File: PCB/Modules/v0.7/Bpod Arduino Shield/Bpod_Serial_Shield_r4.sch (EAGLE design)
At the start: 9 parts, among them IC1 SN65HVD31DR

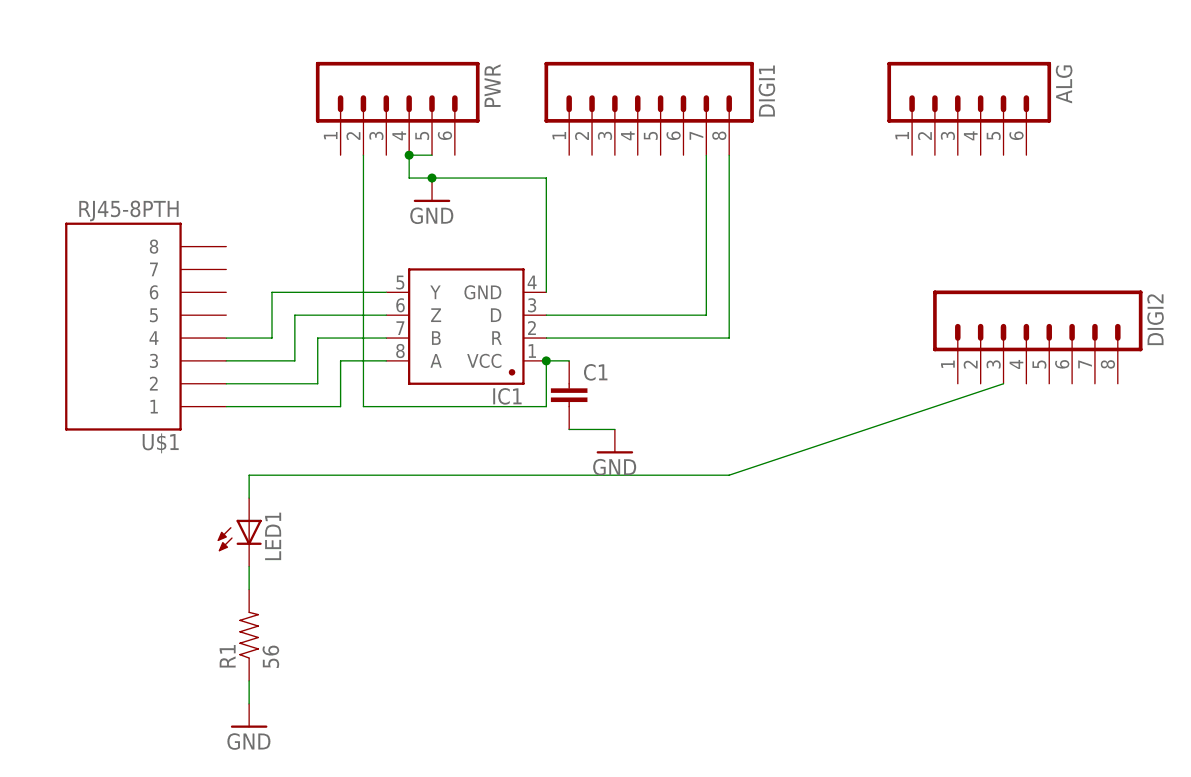
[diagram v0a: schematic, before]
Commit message: -Added design files for the Pocket State Machine - a new state machine module with many improvements, based on Teensy 3.6. -Added design files for isolated valve driver module -Added new revision of Bpod arduino shield, allowing modules to be powered from the Pocket State Machine (when they do not require a USB connection)
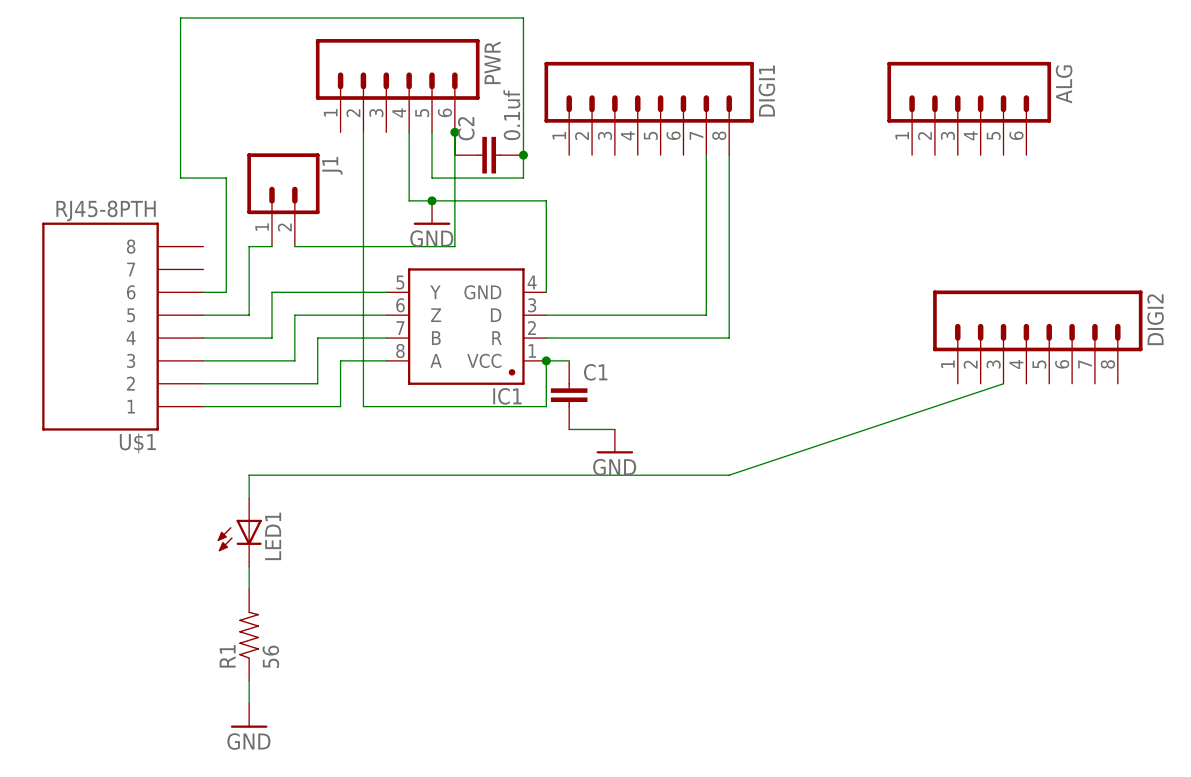
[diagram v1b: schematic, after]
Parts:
- added C2: 0.1uf, SparkFun-Capacitors:CAP1206
- added J1: (no value), SparkFun-Connectors:CONN_02
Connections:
- new net N$11: C2.2, PWR.5, U$1.6
- new net N$12: J1.1, U$1.5
- new net N$5: C2.1, J1.2, PWR.6
- net GND: no longer PWR.5
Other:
- moved on the sheet: PWR, U$1
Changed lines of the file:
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@@
 <?xml version="1.0" encoding="utf-8"?>
 <!DOCTYPE eagle SYSTEM "eagle.dtd">
-<eagle version="7.6.0">
+<eagle version="7.7.0">
 <drawing>
 <settings>
@@
 <layer number="112" name="tSilk" color="7" fill="1" visible="yes" active="yes"/>
 <layer number="113" name="IDFDebug" color="7" fill="1" visible="yes" active="yes"/>
+<layer number="114" name="Badge_Outline" color="7" fill="1" visible="yes" active="yes"/>
+<layer number="115" name="ReferenceISLANDS" color="7" fill="1" visible="yes" active="yes"/>
 <layer number="116" name="Patch_BOT" color="9" fill="4" visible="no" active="yes"/>
 <layer number="118" name="Rect_Pads" color="7" fill="1" visible="yes" active="yes"/>
@@
 <part name="LED1" library="adafruit" deviceset="LED" device="CHIPLED_1206"/>
 <part name="R1" library="SparkFun-Resistors" deviceset="RESISTOR" device="1206" value="56"/>
+<part name="J1" library="SparkFun-Connectors" deviceset="CONN_02" device=""/>
+<part name="C2" library="SparkFun-Capacitors" deviceset="CAP" device="1206" value="0.1uf"/>
 </parts>
 <sheets>
@@
 </plain>
 <instances>
-<instance part="PWR" gate="G$1" x="88.9" y="66.04" rot="R270"/>
+<instance part="PWR" gate="G$1" x="88.9" y="68.58" rot="R270"/>
 <instance part="ALG" gate="G$1" x="152.4" y="66.04" rot="R270"/>
 <instance part="DIGI1" gate="G$1" x="116.84" y="66.04" rot="R270"/>
 <instance part="DIGI2" gate="G$1" x="160.02" y="40.64" rot="R270"/>
-<instance part="U$1" gate="G$1" x="58.42" y="43.18" rot="R180"/>
-<instance part="GND1" gate="1" x="93.98" y="55.88"/>
+<instance part="U$1" gate="G$1" x="55.88" y="43.18" rot="R180"/>
+<instance part="GND1" gate="1" x="93.98" y="53.34"/>
 <instance part="GND2" gate="1" x="73.66" y="-2.54"/>
 <instance part="IC1" gate="G$1" x="104.14" y="38.1" rot="R180"/>
@@
 <instance part="LED1" gate="G$1" x="73.66" y="20.32"/>
 <instance part="R1" gate="G$1" x="73.66" y="7.62" rot="R90"/>
+<instance part="J1" gate="G$1" x="76.2" y="58.42" rot="R270"/>
+<instance part="C2" gate="G$1" x="101.6" y="60.96" rot="R90"/>
 </instances>
 <busses>
@@
 <segment>
 <pinref part="PWR" gate="G$1" pin="4"/>
-<wire x1="91.44" y1="58.42" x2="91.44" y2="60.96" width="0.1524" layer="91"/>
-<pinref part="PWR" gate="G$1" pin="5"/>
-<wire x1="91.44" y1="60.96" x2="93.98" y2="60.96" width="0.1524" layer="91"/>
-<junction x="91.44" y="60.96"/>
+<wire x1="91.44" y1="55.88" x2="91.44" y2="63.5" width="0.1524" layer="91"/>
 <pinref part="GND1" gate="1" pin="GND"/>
-<wire x1="93.98" y1="58.42" x2="91.44" y2="58.42" width="0.1524" layer="91"/>
+<wire x1="93.98" y1="55.88" x2="91.44" y2="55.88" width="0.1524" layer="91"/>
 <pinref part="IC1" gate="G$1" pin="GND"/>
-<wire x1="106.68" y1="45.72" x2="106.68" y2="58.42" width="0.1524" layer="91"/>
-<wire x1="106.68" y1="58.42" x2="93.98" y2="58.42" width="0.1524" layer="91"/>
-<junction x="93.98" y="58.42"/>
+<wire x1="106.68" y1="45.72" x2="106.68" y2="55.88" width="0.1524" layer="91"/>
+<wire x1="106.68" y1="55.88" x2="93.98" y2="55.88" width="0.1524" layer="91"/>
+<junction x="93.98" y="55.88"/>
 </segment>
 <segment>
@@
 <segment>
 <pinref part="PWR" gate="G$1" pin="2"/>
-<wire x1="86.36" y1="60.96" x2="86.36" y2="33.02" width="0.1524" layer="91"/>
+<wire x1="86.36" y1="63.5" x2="86.36" y2="33.02" width="0.1524" layer="91"/>
 <pinref part="IC1" gate="G$1" pin="VCC"/>
 <wire x1="86.36" y1="33.02" x2="106.68" y2="33.02" width="0.1524" layer="91"/>
@@
 <wire x1="83.82" y1="38.1" x2="83.82" y2="33.02" width="0.1524" layer="91"/>
 <pinref part="U$1" gate="G$1" pin="1"/>
-<wire x1="83.82" y1="33.02" x2="71.12" y2="33.02" width="0.1524" layer="91"/>
+<wire x1="83.82" y1="33.02" x2="68.58" y2="33.02" width="0.1524" layer="91"/>
 </segment>
 </net>
@@
 <segment>
 <pinref part="U$1" gate="G$1" pin="2"/>
-<wire x1="71.12" y1="35.56" x2="81.28" y2="35.56" width="0.1524" layer="91"/>
+<wire x1="68.58" y1="35.56" x2="81.28" y2="35.56" width="0.1524" layer="91"/>
 <wire x1="81.28" y1="35.56" x2="81.28" y2="40.64" width="0.1524" layer="91"/>
 <pinref part="IC1" gate="G$1" pin="B"/>
@@
 <segment>
 <pinref part="U$1" gate="G$1" pin="3"/>
-<wire x1="71.12" y1="38.1" x2="78.74" y2="38.1" width="0.1524" layer="91"/>
+<wire x1="68.58" y1="38.1" x2="78.74" y2="38.1" width="0.1524" layer="91"/>
 <wire x1="78.74" y1="38.1" x2="78.74" y2="43.18" width="0.1524" layer="91"/>
 <pinref part="IC1" gate="G$1" pin="Z"/>
@@
 <segment>
 <pinref part="U$1" gate="G$1" pin="4"/>
-<wire x1="71.12" y1="40.64" x2="76.2" y2="40.64" width="0.1524" layer="91"/>
+<wire x1="68.58" y1="40.64" x2="76.2" y2="40.64" width="0.1524" layer="91"/>
 <wire x1="76.2" y1="40.64" x2="76.2" y2="45.72" width="0.1524" layer="91"/>
 <pinref part="IC1" gate="G$1" pin="Y"/>
@@
 </segment>
 </net>
+<net name="N$5" class="0">
+<segment>
+<pinref part="PWR" gate="G$1" pin="6"/>
+<wire x1="96.52" y1="50.8" x2="96.52" y2="63.5" width="0.1524" layer="91"/>
+<pinref part="C2" gate="G$1" pin="1"/>
+<junction x="96.52" y="63.5"/>
+<wire x1="96.52" y1="63.5" x2="96.52" y2="60.96" width="0.1524" layer="91"/>
+<pinref part="J1" gate="G$1" pin="2"/>
+<wire x1="78.74" y1="50.8" x2="96.52" y2="50.8" width="0.1524" layer="91"/>
+</segment>
+</net>
+<net name="N$11" class="0">
+<segment>
+<pinref part="U$1" gate="G$1" pin="6"/>
+<wire x1="68.58" y1="45.72" x2="71.12" y2="45.72" width="0.1524" layer="91"/>
+<wire x1="71.12" y1="45.72" x2="71.12" y2="58.42" width="0.1524" layer="91"/>
+<pinref part="C2" gate="G$1" pin="2"/>
+<wire x1="104.14" y1="60.96" x2="104.14" y2="76.2" width="0.1524" layer="91"/>
+<wire x1="104.14" y1="76.2" x2="66.04" y2="76.2" width="0.1524" layer="91"/>
+<wire x1="66.04" y1="76.2" x2="66.04" y2="58.42" width="0.1524" layer="91"/>
+<wire x1="66.04" y1="58.42" x2="71.12" y2="58.42" width="0.1524" layer="91"/>
+<wire x1="104.14" y1="60.96" x2="104.14" y2="58.42" width="0.1524" layer="91"/>
+<junction x="104.14" y="60.96"/>
+<pinref part="PWR" gate="G$1" pin="5"/>
+<wire x1="104.14" y1="58.42" x2="93.98" y2="58.42" width="0.1524" layer="91"/>
+<wire x1="93.98" y1="58.42" x2="93.98" y2="63.5" width="0.1524" layer="91"/>
+</segment>
+</net>
+<net name="N$12" class="0">
+<segment>
+<wire x1="73.66" y1="43.18" x2="73.66" y2="50.8" width="0.1524" layer="91"/>
+<pinref part="U$1" gate="G$1" pin="5"/>
+<wire x1="68.58" y1="43.18" x2="73.66" y2="43.18" width="0.1524" layer="91"/>
+<pinref part="J1" gate="G$1" pin="1"/>
+<wire x1="73.66" y1="50.8" x2="76.2" y2="50.8" width="0.1524" layer="91"/>
+</segment>
+</net>
